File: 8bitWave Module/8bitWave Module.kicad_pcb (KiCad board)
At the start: 2 copper layers, 99.7 x 64.1 mm, 25 parts, among them IC1 0.96_I2C_OLED, IC2 0.91_I2C_OLED, J1 REM, J2 EAR, M1 Mounting, M2 Mounting, M3 Mounting, M4 Mounting, SW1 UP, SW2 DOWN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

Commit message: Layout sketched out
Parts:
- added C1: 100nF, Capacitors_THT:C_Disc_D4.7mm_W2.5mm_P5.00mm, F.Cu at (128.9, 97.2)
- added C10: 100uF, Capacitors_THT:CP_Radial_D5.0mm_P2.50mm, F.Cu at (95.2, 92.7)
- added C2: 4.7nF, Capacitors_THT:C_Disc_D4.7mm_W2.5mm_P5.00mm, F.Cu at (132.7, 92.1)
- added C3: 4.7nF, Capacitors_THT:C_Disc_D4.7mm_W2.5mm_P5.00mm, F.Cu at (136.5, 92.1)
- added C4: 4.7nF, Capacitors_THT:C_Disc_D4.7mm_W2.5mm_P5.00mm, F.Cu at (140.3, 92.1)
- added C5: 100nF, Capacitors_THT:C_Disc_D4.7mm_W2.5mm_P5.00mm, F.Cu at (118.7, 95.9)
- added C6: 10uF, Capacitors_THT:CP_Radial_D4.0mm_P2.00mm, F.Cu at (113.7, 97.2)
- added C7: 100uF, Capacitors_THT:CP_Radial_D5.0mm_P2.00mm, F.Cu at (112.8, 90.4)
- added C8: 10uF, Capacitors_THT:CP_Radial_D4.0mm_P2.00mm, F.Cu at (99.7, 81.9)
- added C9: 10pF, Capacitors_THT:C_Disc_D4.7mm_W2.5mm_P5.00mm, F.Cu at (80.6, 96.5)
- added D1: POWER, LEDs:LED_D5.0mm, F.Cu at (80.6, 137.2)
- added D2: USER, LEDs:LED_D5.0mm, F.Cu at (160.0, 137.2)
- added J3: Faceplate, Pin_Headers:Pin_Header_Straight_1x08_Pitch2.54mm, F.Cu at (168.9, 87.0)
- added JP4: BYPASS, Pin_Headers:Pin_Header_Straight_1x02_Pitch2.54mm, F.Cu at (114.9, 85.1)
- added R6: 220, Resistors_THT:R_Axial_DIN0207_L6.3mm_D2.5mm_P10.16mm_Horizontal, F.Cu at (158.8, 126.4)
- added R7: 220, Resistors_THT:R_Axial_DIN0207_L6.3mm_D2.5mm_P10.16mm_Horizontal, F.Cu at (158.8, 130.2)
- A2: value SD -> MicroSD
- moved J1 78.4 mm to (93.3, 78.7)
- moved JP3 77.5 mm to (72.4, 91.4), turned to 180 degrees
- moved J2 76.1 mm to (83.2, 84.5)
- moved R3 75.6 mm to (140.3, 79.4), turned to 270 degrees
- moved R2 74.7 mm to (136.5, 79.4), turned to 270 degrees
- moved R1 74.0 mm to (132.7, 79.4), turned to 270 degrees
- moved JP1 73.8 mm to (105.4, 80.0), turned to 90 degrees
- moved R4 73.4 mm to (128.9, 79.4), turned to 270 degrees
- moved R5 73.0 mm to (78.1, 92.7)
- moved JP2 72.7 mm to (112.4, 80.0), turned to 90 degrees
- moved U1 68.9 mm to (100.3, 86.4)
- moved RV1 65.3 mm to (120.0, 87.0)
- moved A1 41.1 mm to (161.3, 117.5), turned to 180 degrees
- moved IC2 31.5 mm to (102.2, 104.8)
- moved A2 31.2 mm to (109.2, 123.2)
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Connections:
- A1 pad 11: (no net) -> /D8
- A1 pad 5: (no net) -> /D2
- A1 pad 6: (no net) -> /USER
- A1 pad 7: (no net) -> /D4
- A1 pad 8: (no net) -> /POWER
- J1 pad 2: (no net) -> /REM
- J1 pad 3: /REM -> (no net)
- JP1 pad 1: (no net) -> Net-(C8-Pad2)
- JP2 pad 1: Net-(C1-Pad2) -> /SOUND
- JP2 pad 2: /SOUND -> Net-(C1-Pad2)
- JP3 pad 1: (no net) -> Net-(C10-Pad2)
- R1 pad 2: (no net) -> Net-(C1-Pad1)
- R5 pad 2: (no net) -> Net-(C9-Pad2)
- U1 pad 1: (no net) -> Net-(C8-Pad1)
- U1 pad 5: (no net) -> Net-(C10-Pad1)
- U1 pad 7: (no net) -> Net-(C7-Pad1)
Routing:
- net /SOUND: track 0.00 -> 108.4 mm, vias 0 -> 1
- net /PLAY: track 0.00 -> 108.3 mm, vias 0 -> 2
- net +5V: track 0.00 -> 104.1 mm, vias 0 -> 2
- net /STOP: track 0.00 -> 96.8 mm, vias 0 -> 2
- net /REM: track 0.00 -> 96.3 mm, vias 0 -> 5
- net +3V3: track 0.00 -> 95.9 mm, vias 0 -> 2
- net Net-(D1-Pad2): track 0.00 -> 94.1 mm
- net /CS: track 0.00 -> 93.1 mm, vias 0 -> 2
- net /MOSI: track 0.00 -> 90.6 mm, vias 0 -> 3
- net /MISO: track 0.00 -> 90.6 mm, vias 0 -> 3
- net /ROOT: track 0.00 -> 82.3 mm, vias 0 -> 2
- net /SCK: track 0.00 -> 80.4 mm, vias 0 -> 2
- net /SDA: track 0.00 -> 78.2 mm
- net /UP: track 0.00 -> 74.2 mm, vias 0 -> 2
- net /SCL: track 0.00 -> 73.8 mm, vias 0 -> 2
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- added copper zone on B.Cu, net GND

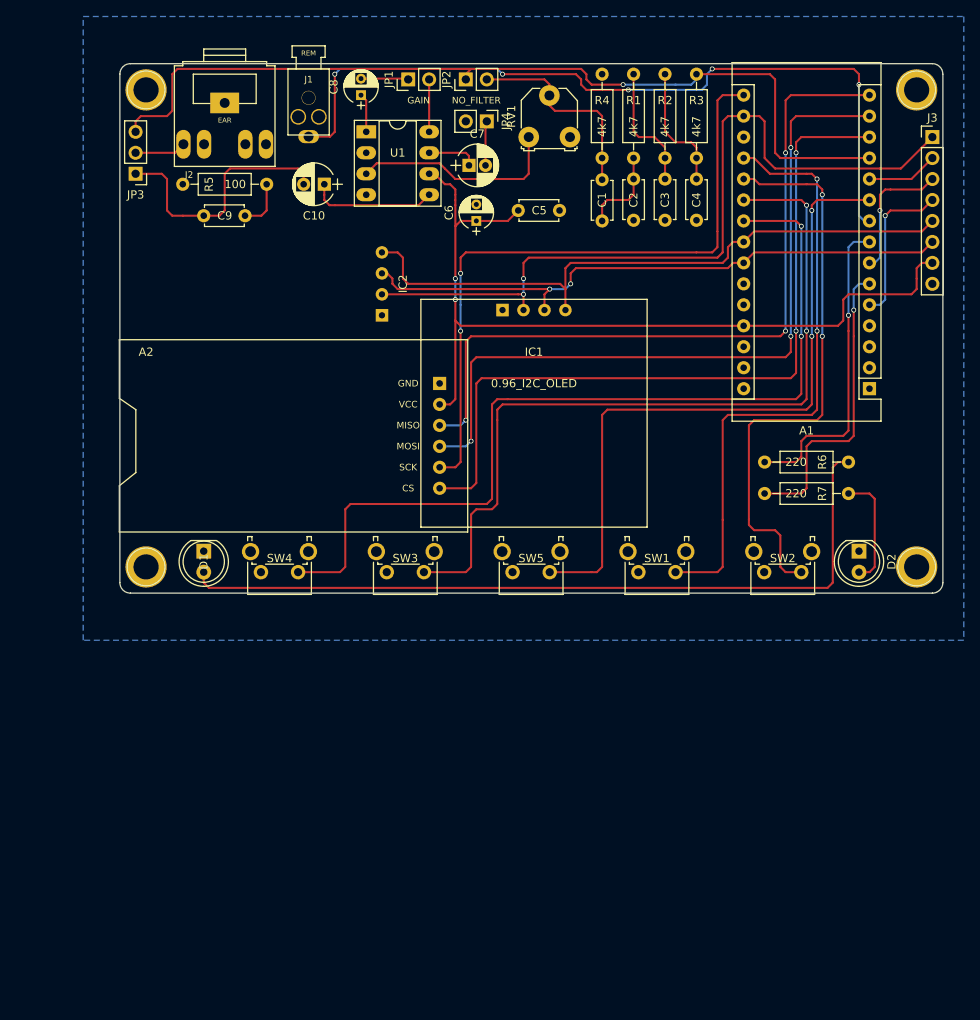
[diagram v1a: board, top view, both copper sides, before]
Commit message: Tweaked silkscreen
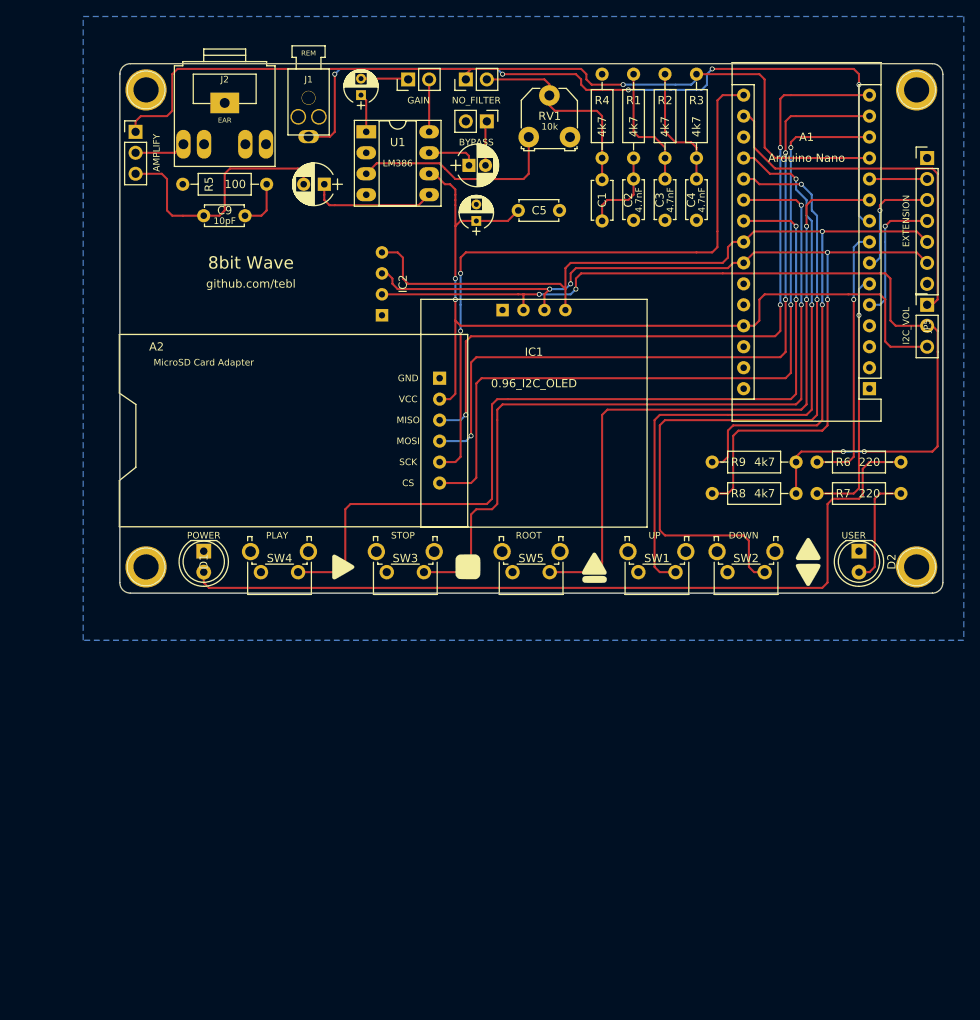
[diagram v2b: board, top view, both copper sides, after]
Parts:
- added G***: LOGO, icons:updown, F.Cu at (153.7, 138.4)
- added G***: LOGO, icons:play, F.Cu at (97.5, 139.2)
- added G***: LOGO, icons:stop, F.Cu at (112.8, 139.2)
- added G***: LOGO, icons:eject, F.Cu at (127.8, 140.2)
- added JP5: I2C_VOL, Pin_Headers:Pin_Header_Straight_1x03_Pitch2.54mm, F.Cu at (168.3, 107.3)
- added R8: 4k7, Resistors_THT:R_Axial_DIN0207_L6.3mm_D2.5mm_P10.16mm_Horizontal, F.Cu at (142.2, 130.2)
- added R9: 4k7, Resistors_THT:R_Axial_DIN0207_L6.3mm_D2.5mm_P10.16mm_Horizontal, F.Cu at (142.2, 126.4)
- A1: value Arduino_Nano_v3.x -> Arduino Nano
- A2: value MicroSD -> MicroSD Card Adapter
- J3: value Faceplate -> EXTENSION; footprint Pin_Headers:Pin_Header_Straight_1x08_Pitch2.54mm -> Pin_Headers:Pin_Header_Straight_1x07_Pitch2.54mm
- moved R6 6.35 mm to (165.1, 126.4)
- moved R7 6.35 mm to (165.1, 130.2)
- moved JP3 5.08 mm to (72.4, 86.4), turned to 0 degrees
- moved SW2 4.44 mm to (148.6, 139.7)
- moved J3 2.62 mm to (168.3, 89.5)
- moved A2 0.63 mm to (109.2, 122.6)
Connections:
- IC1 pad 2: +3V3 -> Net-(IC1-Pad2)
- IC2 pad 2: +3V3 -> Net-(IC1-Pad2)
- J3 pad 1: +3V3 -> GND
- J3 pad 7: +5V -> GND
- JP3 pad 1: Net-(C10-Pad2) -> /SOUND
- JP3 pad 3: /SOUND -> Net-(C10-Pad2)
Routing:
- net Net-(IC1-Pad2): track 0.00 -> 113.0 mm, vias 0 -> 4
- net +3V3: track 95.9 -> 45.0 mm, vias 2 -> 0
- net /SCL: track 73.8 -> 115.2 mm, vias 2 -> 4
- net /SDA: track 78.2 -> 117.7 mm, vias 0 -> 2
- net /DOWN: track 69.8 -> 84.9 mm
- net /POWER: track 37.9 -> 32.3 mm
- net /USER: track 36.6 -> 31.0 mm
- net Net-(D1-Pad2): track 94.1 -> 99.7 mm
- net /UP: track 74.2 -> 76.9 mm
- net /D2: track 18.8 -> 16.4 mm
- net /D4: track 16.3 -> 13.9 mm
- net /D8: track 8.67 -> 6.99 mm
- net +5V: track 104.1 -> 105.4 mm
- net /PLAY: track 108.3 -> 107.0 mm
- net /STOP: track 96.8 -> 95.6 mm
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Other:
- board text added: "1-2 3.3v 2-3 5v"
- board text added: "1-2 Direct 2-3 Amplified"
- board text added: "8bit Wave"
- board text added: "I2C PULL-UP"
- board text added: "github.com/tebl"
